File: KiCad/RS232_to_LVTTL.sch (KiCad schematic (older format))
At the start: 11 parts, among them J1 DB25_Female, J2 Conn_01x05, U1 TPS54308, U2 MAX3232

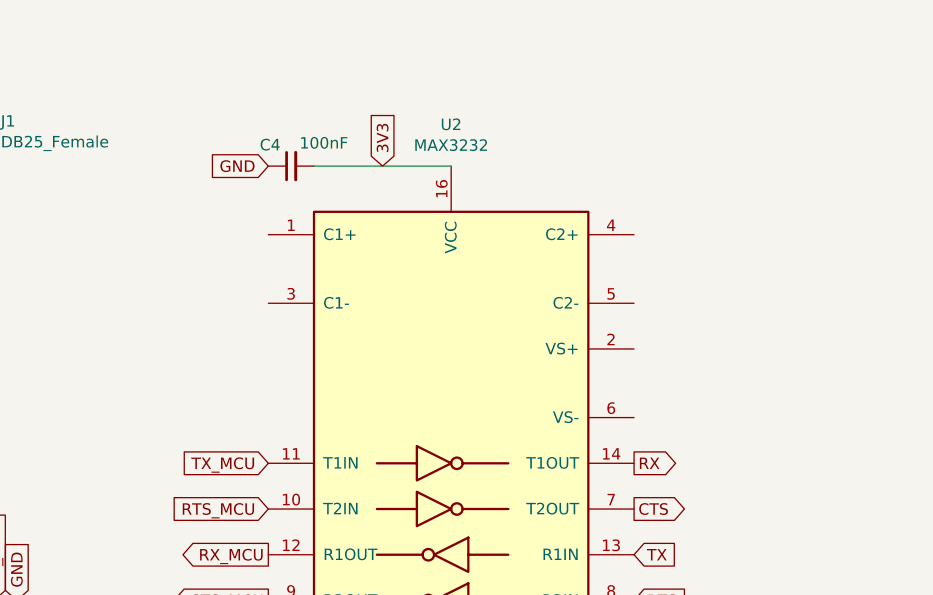
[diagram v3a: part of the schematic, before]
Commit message: Fixed positioning of 5-pin header
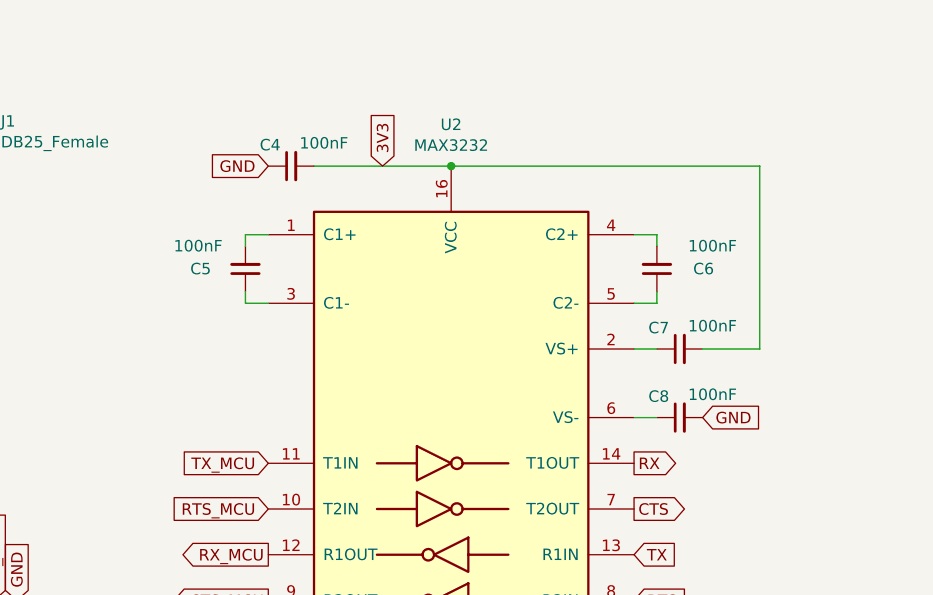
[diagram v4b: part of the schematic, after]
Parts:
- added C5, C6, C7, C8: 100nF, Capacitor_SMD:C_0603_1608Metric_Pad1.05x0.95mm_HandSolder, symbol Device:C_Small
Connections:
- net 3V3: now also C7.2
- net GND: now also C8.2
- net at U2.1 (C1+): now also C5.2
- net at U2.2 (VS+): now also C7.1
- net at U2.3 (C1-): now also C5.1
- net at U2.4 (C2+): now also C6.2
- net at U2.5 (C2-): now also C6.1
- net at U2.6 (VS-): now also C8.1
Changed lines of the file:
@@
 Text GLabel 3300 5200 1    50   Input ~ 0
 GND
+$Comp
+L Device:C_Small C7
+U 1 1 642A667C
+P 6200 4100
+F 0 "C7" V 6292 4146 50  0000 L CNN
+F 1 "100nF" V 6300 3850 50  0000 L CNN
+F 2 "Capacitor_SMD:C_0603_1608Metric_Pad1.05x0.95mm_HandSolder" H 6200 4100 50  0001 C CNN
+F 3 "~" H 6200 4100 50  0001 C CNN
+	1    6200 4100
+	0    -1   -1   0
+$EndComp
+Wire Wire Line
+	4400 3600 4300 3600
+Wire Wire Line
+	4300 3600 4300 3650
+Wire Wire Line
+	4400 3900 4300 3900
+Wire Wire Line
+	4300 3900 4300 3850
+Wire Wire Line
+	6000 3600 6100 3600
+Wire Wire Line
+	6100 3600 6100 3650
+Wire Wire Line
+	6000 3900 6100 3900
+Wire Wire Line
+	6100 3900 6100 3850
+$Comp
+L Device:C_Small C8
+U 1 1 642AFA1A
+P 6200 4400
+F 0 "C8" V 6292 4446 50  0000 L CNN
+F 1 "100nF" V 6300 4150 50  0000 L CNN
+F 2 "Capacitor_SMD:C_0603_1608Metric_Pad1.05x0.95mm_HandSolder" H 6200 4400 50  0001 C CNN
+F 3 "~" H 6200 4400 50  0001 C CNN
+	1    6200 4400
+	0    -1   -1   0
+$EndComp
+$Comp
+L Device:C_Small C5
+U 1 1 642A7281
+P 4300 3750
+F 0 "C5" H 4450 3750 50  0000 L CNN
+F 1 "100nF" H 4400 3650 50  0000 L CNN
+F 2 "Capacitor_SMD:C_0603_1608Metric_Pad1.05x0.95mm_HandSolder" H 4300 3750 50  0001 C CNN
+F 3 "~" H 4300 3750 50  0001 C CNN
+	1    4300 3750
+	-1   0    0    1
+$EndComp
+$Comp
+L Device:C_Small C6
+U 1 1 642AA23A
+P 6100 3750
+F 0 "C6" H 5850 3750 50  0000 L CNN
+F 1 "100nF" H 5750 3650 50  0000 L CNN
+F 2 "Capacitor_SMD:C_0603_1608Metric_Pad1.05x0.95mm_HandSolder" H 6100 3750 50  0001 C CNN
+F 3 "~" H 6100 3750 50  0001 C CNN
+	1    6100 3750
+	-1   0    0    1
+$EndComp
+Wire Wire Line
+	6000 4100 6100 4100
+Wire Wire Line
+	6300 4100 6550 4100
+Wire Wire Line
+	6550 4100 6550 3300
+Wire Wire Line
+	6550 3300 5200 3300
+Connection ~ 5200 3300
+Wire Wire Line
+	6000 4400 6100 4400
+Text GLabel 6300 4400 2    50   Input ~ 0
+GND
 $EndSCHEMATC

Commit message: routing and placing of components
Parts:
- added D1, D2: LED, Diode_SMD:D_0603_1608Metric_Pad1.05x0.95mm_HandSolder, symbol Device:LED
- added R3, R4: 1k, Resistor_SMD:R_0603_1608Metric_Pad1.05x0.95mm_HandSolder, symbol Device:R_Small
- renumbered C7 to C6, C6 to C7
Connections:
- net 3V3: now also C4.1, R3.1, R4.1; no longer C4.2
- net GND: now also C4.2; no longer C4.1
- net RX_MCU: now also D1.1 (K)
- net TX_MCU: now also D2.1 (K)
- new net: D2.2 (A), R4.2
- new net: D1.2 (A), R3.2
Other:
- moved on the sheet: C4, C5, C6, C7, C8, J2, U2
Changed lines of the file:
@@
 L Interface_UART:MAX3232 U2
 U 1 1 64282C45
-P 5200 4500
-F 0 "U2" H 5200 5881 50  0000 C CNN
-F 1 "MAX3232" H 5200 5790 50  0000 C CNN
-F 2 "Package_SO:TSSOP-16_4.4x5mm_P0.65mm" H 5250 3450 50  0001 L CNN
-F 3 "https://datasheets.maximintegrated.com/en/ds/MAX3222-MAX3241.pdf" H 5200 4600 50  0001 C CNN
-	1    5200 4500
+P 6050 4500
+F 0 "U2" H 6050 5881 50  0000 C CNN
+F 1 "MAX3232" H 6050 5790 50  0000 C CNN
+F 2 "Package_SO:TSSOP-16_4.4x5mm_P0.65mm" H 6100 3450 50  0001 L CNN
+F 3 "https://datasheets.maximintegrated.com/en/ds/MAX3222-MAX3241.pdf" H 6050 4600 50  0001 C CNN
+	1    6050 4500
 	1    0    0    -1
 $EndComp
@@
 L Device:C_Small C4
 U 1 1 6428B97E
-P 4500 3300
-F 0 "C4" V 4592 3346 50  0000 L CNN
-F 1 "100nF" V 4600 3050 50  0000 L CNN
-F 2 "Capacitor_SMD:C_0805_2012Metric_Pad1.15x1.40mm_HandSolder" H 4500 3300 50  0001 C CNN
-F 3 "~" H 4500 3300 50  0001 C CNN
-	1    4500 3300
-	0    -1   -1   0
-$EndComp
-Text GLabel 4900 3300 1    50   Input ~ 0
+P 5700 3200
+F 0 "C4" H 5850 3200 50  0000 L CNN
+F 1 "100nF" H 5800 3100 50  0000 L CNN
+F 2 "Capacitor_SMD:C_0805_2012Metric_Pad1.15x1.40mm_HandSolder" H 5700 3200 50  0001 C CNN
+F 3 "~" H 5700 3200 50  0001 C CNN
+	1    5700 3200
+	-1   0    0    1
+$EndComp
+Text GLabel 6400 3300 1    50   Input ~ 0
 3V3
-Wire Wire Line
-	4600 3300 5200 3300
-Text GLabel 4400 3300 0    50   Input ~ 0
-GND
-Text GLabel 6000 4600 2    50   Output ~ 0
+Text GLabel 5700 3100 1    50   Input ~ 0
+GND
+Text GLabel 6850 4600 2    50   Output ~ 0
 RX
-Text GLabel 6000 5000 2    50   Input ~ 0
+Text GLabel 6850 5000 2    50   Input ~ 0
 TX
-Text GLabel 6000 5200 2    50   Input ~ 0
+Text GLabel 6850 5200 2    50   Input ~ 0
 RTS
-Text GLabel 6000 4800 2    50   Output ~ 0
+Text GLabel 6850 4800 2    50   Output ~ 0
 CTS
-Text GLabel 4400 4600 0    50   Input ~ 0
+Text GLabel 4900 4600 0    50   Input ~ 0
 TX_MCU
 Text GLabel 4400 5000 0    50   Output ~ 0
 RX_MCU
-Text GLabel 4400 4800 0    50   Input ~ 0
+Text GLabel 5250 4800 0    50   Input ~ 0
 RTS_MCU
-Text GLabel 4400 5200 0    50   Output ~ 0
+Text GLabel 5250 5200 0    50   Output ~ 0
 CTS_MCU
-Text GLabel 5200 5700 3    50   Input ~ 0
+Text GLabel 6050 5700 3    50   Input ~ 0
 GND
 $Comp
 L Connector_Generic:Conn_01x05 J2
 U 1 1 6429DBB7
-P 3100 5400
-F 0 "J2" V 2972 5680 50  0000 L CNN
-F 1 "Conn_01x05" V 3063 5680 50  0000 L CNN
-F 2 "Connector_PinHeader_2.54mm:PinHeader_1x05_P2.54mm_Vertical" H 3100 5400 50  0001 C CNN
-F 3 "~" H 3100 5400 50  0001 C CNN
-	1    3100 5400
-	0    1    1    0
-$EndComp
-Text GLabel 2900 5200 1    50   Input ~ 0
+P 3250 4900
+F 0 "J2" V 3122 5180 50  0000 L CNN
+F 1 "Conn_01x05" V 3213 5180 50  0000 L CNN
+F 2 "Connector_PinHeader_2.54mm:PinHeader_1x05_P2.54mm_Vertical" H 3250 4900 50  0001 C CNN
+F 3 "~" H 3250 4900 50  0001 C CNN
+	1    3250 4900
+	0    -1   -1   0
+$EndComp
+Text GLabel 3450 5100 3    50   Input ~ 0
 CTS_MCU
-Text GLabel 3000 5200 1    50   Output ~ 0
+Text GLabel 3350 5100 3    50   Output ~ 0
 RTS_MCU
-Text GLabel 3100 5200 1    50   Output ~ 0
+Text GLabel 3250 5100 3    50   Output ~ 0
 TX_MCU
-Text GLabel 3200 5200 1    50   Input ~ 0
+Text GLabel 3150 5100 3    50   Input ~ 0
 RX_MCU
-Text GLabel 3300 5200 1    50   Input ~ 0
-GND
-$Comp
-L Device:C_Small C7
+Text GLabel 3050 5100 3    50   Input ~ 0
+GND
+$Comp
+L Device:C_Small C6
 U 1 1 642A667C
-P 6200 4100
-F 0 "C7" V 6292 4146 50  0000 L CNN
-F 1 "100nF" V 6300 3850 50  0000 L CNN
-F 2 "Capacitor_SMD:C_0603_1608Metric_Pad1.05x0.95mm_HandSolder" H 6200 4100 50  0001 C CNN
-F 3 "~" H 6200 4100 50  0001 C CNN
-	1    6200 4100
-	0    -1   -1   0
-$EndComp
-Wire Wire Line
-	4400 3600 4300 3600
-Wire Wire Line
-	4300 3600 4300 3650
-Wire Wire Line
-	4400 3900 4300 3900
-Wire Wire Line
-	4300 3900 4300 3850
-Wire Wire Line
-	6000 3600 6100 3600
-Wire Wire Line
-	6100 3600 6100 3650
-Wire Wire Line
-	6000 3900 6100 3900
-Wire Wire Line
-	6100 3900 6100 3850
+P 7050 4100
+F 0 "C6" V 7142 4146 50  0000 L CNN
+F 1 "100nF" V 7150 3850 50  0000 L CNN
+F 2 "Capacitor_SMD:C_0603_1608Metric_Pad1.05x0.95mm_HandSolder" H 7050 4100 50  0001 C CNN
+F 3 "~" H 7050 4100 50  0001 C CNN
+	1    7050 4100
+	0    -1   -1   0
+$EndComp
+Wire Wire Line
+	5250 3600 5150 3600
+Wire Wire Line
+	5150 3600 5150 3650
+Wire Wire Line
+	5250 3900 5150 3900
+Wire Wire Line
+	5150 3900 5150 3850
+Wire Wire Line
+	6850 3600 6950 3600
+Wire Wire Line
+	6950 3600 6950 3650
+Wire Wire Line
+	6850 3900 6950 3900
+Wire Wire Line
+	6950 3900 6950 3850
 $Comp
 L Device:C_Small C8
 U 1 1 642AFA1A
-P 6200 4400
-F 0 "C8" V 6292 4446 50  0000 L CNN
-F 1 "100nF" V 6300 4150 50  0000 L CNN
-F 2 "Capacitor_SMD:C_0603_1608Metric_Pad1.05x0.95mm_HandSolder" H 6200 4400 50  0001 C CNN
-F 3 "~" H 6200 4400 50  0001 C CNN
-	1    6200 4400
+P 7050 4400
+F 0 "C8" V 7142 4446 50  0000 L CNN
+F 1 "100nF" V 7150 4150 50  0000 L CNN
+F 2 "Capacitor_SMD:C_0603_1608Metric_Pad1.05x0.95mm_HandSolder" H 7050 4400 50  0001 C CNN
+F 3 "~" H 7050 4400 50  0001 C CNN
+	1    7050 4400
 	0    -1   -1   0
 $EndComp
@@
 L Device:C_Small C5
 U 1 1 642A7281
-P 4300 3750
-F 0 "C5" H 4450 3750 50  0000 L CNN
-F 1 "100nF" H 4400 3650 50  0000 L CNN
-F 2 "Capacitor_SMD:C_0603_1608Metric_Pad1.05x0.95mm_HandSolder" H 4300 3750 50  0001 C CNN
-F 3 "~" H 4300 3750 50  0001 C CNN
-	1    4300 3750
+P 5150 3750
+F 0 "C5" H 5200 3650 50  0000 L CNN
+F 1 "100nF" H 5100 3550 50  0000 L CNN
+F 2 "Capacitor_SMD:C_0603_1608Metric_Pad1.05x0.95mm_HandSolder" H 5150 3750 50  0001 C CNN
+F 3 "~" H 5150 3750 50  0001 C CNN
+	1    5150 3750
 	-1   0    0    1
 $EndComp
 $Comp
-L Device:C_Small C6
+L Device:C_Small C7
 U 1 1 642AA23A
-P 6100 3750
-F 0 "C6" H 5850 3750 50  0000 L CNN
-F 1 "100nF" H 5750 3650 50  0000 L CNN
-F 2 "Capacitor_SMD:C_0603_1608Metric_Pad1.05x0.95mm_HandSolder" H 6100 3750 50  0001 C CNN
-F 3 "~" H 6100 3750 50  0001 C CNN
-	1    6100 3750
+P 6950 3750
+F 0 "C7" H 6700 3750 50  0000 L CNN
+F 1 "100nF" H 6600 3650 50  0000 L CNN
+F 2 "Capacitor_SMD:C_0603_1608Metric_Pad1.05x0.95mm_HandSolder" H 6950 3750 50  0001 C CNN
+F 3 "~" H 6950 3750 50  0001 C CNN
+	1    6950 3750
 	-1   0    0    1
 $EndComp
 Wire Wire Line
-	6000 4100 6100 4100
-Wire Wire Line
-	6300 4100 6550 4100
-Wire Wire Line
-	6550 4100 6550 3300
-Wire Wire Line
-	6550 3300 5200 3300
-Connection ~ 5200 3300
-Wire Wire Line
-	6000 4400 6100 4400
-Text GLabel 6300 4400 2    50   Input ~ 0
-GND
+	6850 4100 6950 4100
+Wire Wire Line
+	7150 4100 7400 4100
+Wire Wire Line
+	7400 4100 7400 3300
+Wire Wire Line
+	7400 3300 6050 3300
+Connection ~ 6050 3300
+Wire Wire Line
+	6850 4400 6950 4400
+Text GLabel 7150 4400 2    50   Input ~ 0
+GND
+$Comp
+L Device:R_Small R4
+U 1 1 642C12CA
+P 4900 3900
+F 0 "R4" H 4750 3950 50  0000 L CNN
+F 1 "1k" H 4750 3850 50  0000 L CNN
+F 2 "Resistor_SMD:R_0603_1608Metric_Pad1.05x0.95mm_HandSolder" H 4900 3900 50  0001 C CNN
+F 3 "~" H 4900 3900 50  0001 C CNN
+	1    4900 3900
+	1    0    0    -1
+$EndComp
+$Comp
+L Device:R_Small R3
+U 1 1 642C874A
+P 4400 3900
+F 0 "R3" H 4459 3946 50  0000 L CNN
+F 1 "1k" H 4459 3855 50  0000 L CNN
+F 2 "Resistor_SMD:R_0603_1608Metric_Pad1.05x0.95mm_HandSolder" H 4400 3900 50  0001 C CNN
+F 3 "~" H 4400 3900 50  0001 C CNN
+	1    4400 3900
+	1    0    0    -1
+$EndComp
+$Comp
+L Device:LED D2
+U 1 1 642CF70A
+P 4900 4250
+F 0 "D2" V 4939 4133 50  0000 R CNN
+F 1 "LED" V 4848 4133 50  0000 R CNN
+F 2 "Diode_SMD:D_0603_1608Metric_Pad1.05x0.95mm_HandSolder" H 4900 4250 50  0001 C CNN
+F 3 "~" H 4900 4250 50  0001 C CNN
+	1    4900 4250
+	0    -1   -1   0
+$EndComp
+Wire Wire Line
+	5250 4600 4900 4600
+Wire Wire Line
+	4900 4600 4900 4400
+Wire Wire Line
+	4400 5000 5250 5000
+$Comp
+L Device:LED D1
+U 1 1 642D846F
+P 4400 4250
+F 0 "D1" V 4439 4133 50  0000 R CNN
+F 1 "LED" V 4348 4133 50  0000 R CNN
+F 2 "Diode_SMD:D_0603_1608Metric_Pad1.05x0.95mm_HandSolder" H 4400 4250 50  0001 C CNN
+F 3 "~" H 4400 4250 50  0001 C CNN
+	1    4400 4250
+	0    -1   -1   0
+$EndComp
+Wire Wire Line
+	4400 3300 4900 3300
+Wire Wire Line
+	4900 4000 4900 4100
+Wire Wire Line
+	4400 4000 4400 4100
+Wire Wire Line
+	4400 3800 4400 3300
+Wire Wire Line
+	4900 3800 4900 3300
+Connection ~ 4900 3300
+Wire Wire Line
+	4400 4400 4400 5000
+Connection ~ 5700 3300
+Wire Wire Line
+	5700 3300 6050 3300
+Wire Wire Line
+	4900 3300 5700 3300
 $EndSCHEMATC

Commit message: Added a PWR LED and some final routing and silkscreen fixes
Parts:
- added D3: LED, Diode_SMD:D_0603_1608Metric_Pad1.05x0.95mm_HandSolder, symbol Device:LED
- added R5: 1k, Resistor_SMD:R_0603_1608Metric_Pad1.05x0.95mm_HandSolder, symbol Device:R_Small
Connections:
- net 3V3: now also R5.1
- net GND: now also D3.1 (K)
- new net: D3.2 (A), R5.2
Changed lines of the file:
@@
 Wire Wire Line
 	4900 3300 5700 3300
+$Comp
+L Device:LED D3
+U 1 1 64373985
+P 3900 4250
+F 0 "D3" V 3939 4133 50  0000 R CNN
+F 1 "LED" V 3848 4133 50  0000 R CNN
+F 2 "Diode_SMD:D_0603_1608Metric_Pad1.05x0.95mm_HandSolder" H 3900 4250 50  0001 C CNN
+F 3 "~" H 3900 4250 50  0001 C CNN
+	1    3900 4250
+	0    -1   -1   0
+$EndComp
+$Comp
+L Device:R_Small R5
+U 1 1 64374459
+P 3900 3900
+F 0 "R5" H 3959 3946 50  0000 L CNN
+F 1 "1k" H 3959 3855 50  0000 L CNN
+F 2 "Resistor_SMD:R_0603_1608Metric_Pad1.05x0.95mm_HandSolder" H 3900 3900 50  0001 C CNN
+F 3 "~" H 3900 3900 50  0001 C CNN
+	1    3900 3900
+	1    0    0    -1
+$EndComp
+Wire Wire Line
+	3900 3800 3900 3300
+Connection ~ 4400 3300
+Wire Wire Line
+	3900 4100 3900 4000
+Text GLabel 3900 4600 3    50   Input ~ 0
+GND
+Wire Wire Line
+	3900 4600 3900 4400
+Wire Wire Line
+	3900 3300 4400 3300
 $EndSCHEMATC

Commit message: some small routing and silkscreen fixes
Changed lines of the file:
@@
 	0    -1   -1   0
 $EndComp
-Text GLabel 3450 5100 3    50   Input ~ 0
-CTS_MCU
-Text GLabel 3350 5100 3    50   Output ~ 0
-RTS_MCU
-Text GLabel 3250 5100 3    50   Output ~ 0
-TX_MCU
-Text GLabel 3150 5100 3    50   Input ~ 0
-RX_MCU
 Text GLabel 3050 5100 3    50   Input ~ 0
 GND
@@
 Wire Wire Line
 	3900 3300 4400 3300
+Text GLabel 3350 5100 3    50   Output ~ 0
+RTS_MCU
+Text GLabel 3450 5100 3    50   Input ~ 0
+CTS_MCU
+Text GLabel 3150 5100 3    50   Output ~ 0
+RX_MCU
+Text GLabel 3250 5100 3    50   Input ~ 0
+TX_MCU
 $EndSCHEMATC
